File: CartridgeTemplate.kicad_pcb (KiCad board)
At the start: 2 copper layers, 64.8 x 55.9 mm, 3 parts, among them J1 Cartridge Connector, U1 W25Q128

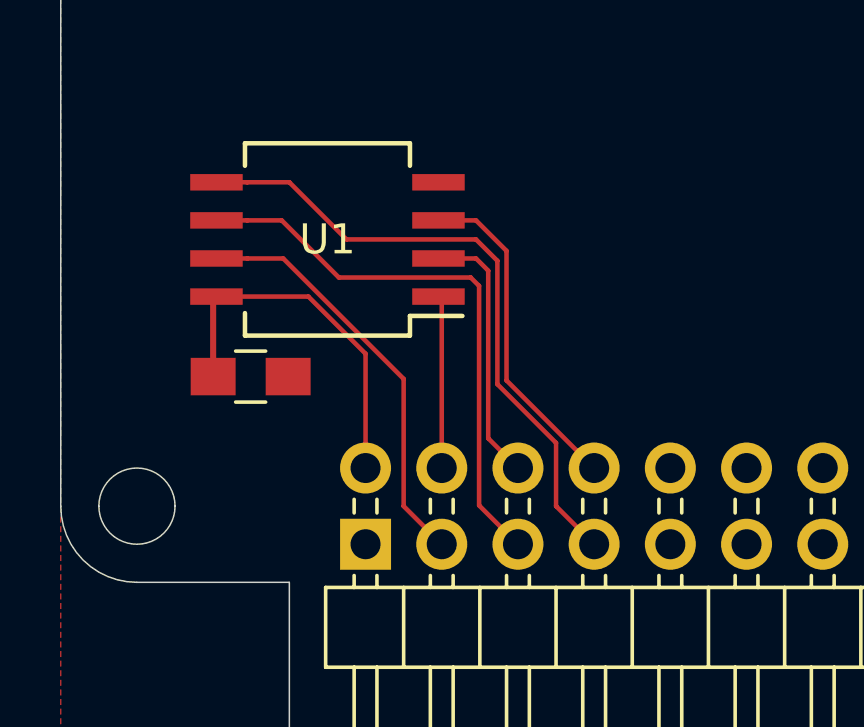
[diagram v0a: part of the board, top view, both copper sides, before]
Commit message: Fixed error in cartridge connector pin assignments
Also added copper pour on bottom layer

Updated to version 1.2
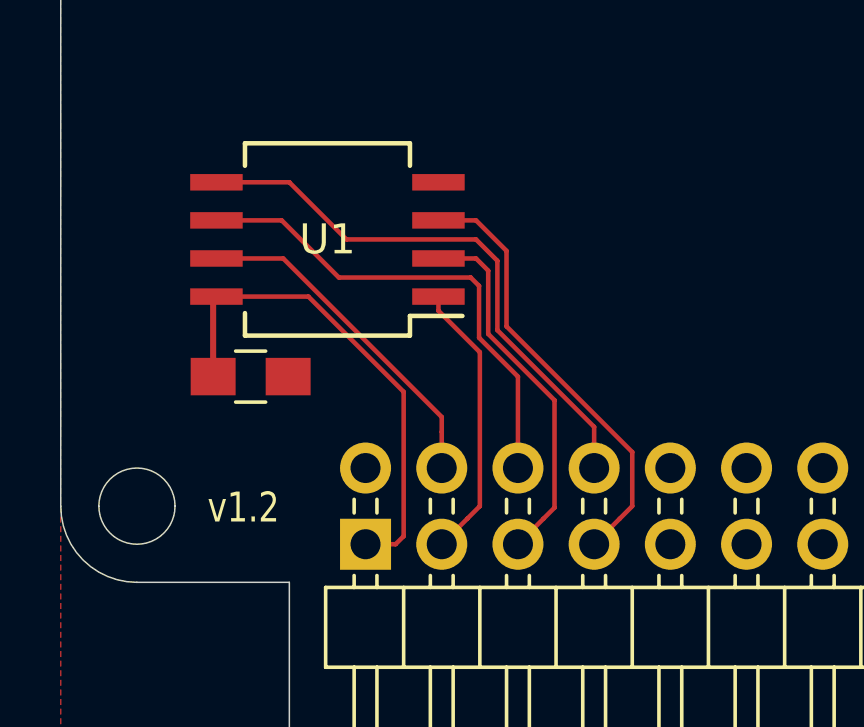
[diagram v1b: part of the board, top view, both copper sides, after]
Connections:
- J1 pad 1: GND -> +3V3
- J1 pad 2: +3V3 -> GND
- J1 pad 3: F_HOLD -> F_CS
- J1 pad 39: +5V -> +BATT
- J1 pad 4: F_CS -> F_HOLD
- J1 pad 40: +BATT -> +5V
- J1 pad 5: F_SCK -> F_MISO
- J1 pad 6: F_MISO -> F_SCK
- J1 pad 7: F_MOSI -> F_WP
- J1 pad 8: F_WP -> F_MOSI
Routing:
- net +3V3: track 12.3 -> 16.5 mm
- net F_CS: track 5.76 -> 9.51 mm
- net F_WP: track 11.1 -> 14.7 mm
- net F_MISO: track 8.82 -> 12.4 mm
- net F_MOSI: track 21.2 -> 18.7 mm
- net F_HOLD: track 13.9 -> 11.4 mm
- net F_SCK: track 18.8 -> 16.3 mm
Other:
- net class Default: clearance 0.2 -> 0.1524
- rule trace_clearance: 0.2 -> 0.1524
- rule trace_min: 0.2 -> 0.1524
- board text added: "v1.2"
